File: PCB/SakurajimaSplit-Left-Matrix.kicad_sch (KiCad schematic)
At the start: 42 parts, among them SW10 S, SW11 D, SW12 F, SW13 G, SW14 SW_Push_45deg, SW15 Z, SW16 X, SW17 C, SW18 V, SW19 B, SW2 ESC, SW20 SW_Push_45deg, SW21 SW_Push_45deg, SW22 SW_Push_45deg, SW3 Q, SW4 W, SW5 E, SW6 R, SW7 T, SW8 SW_Push_45deg, SW9 A

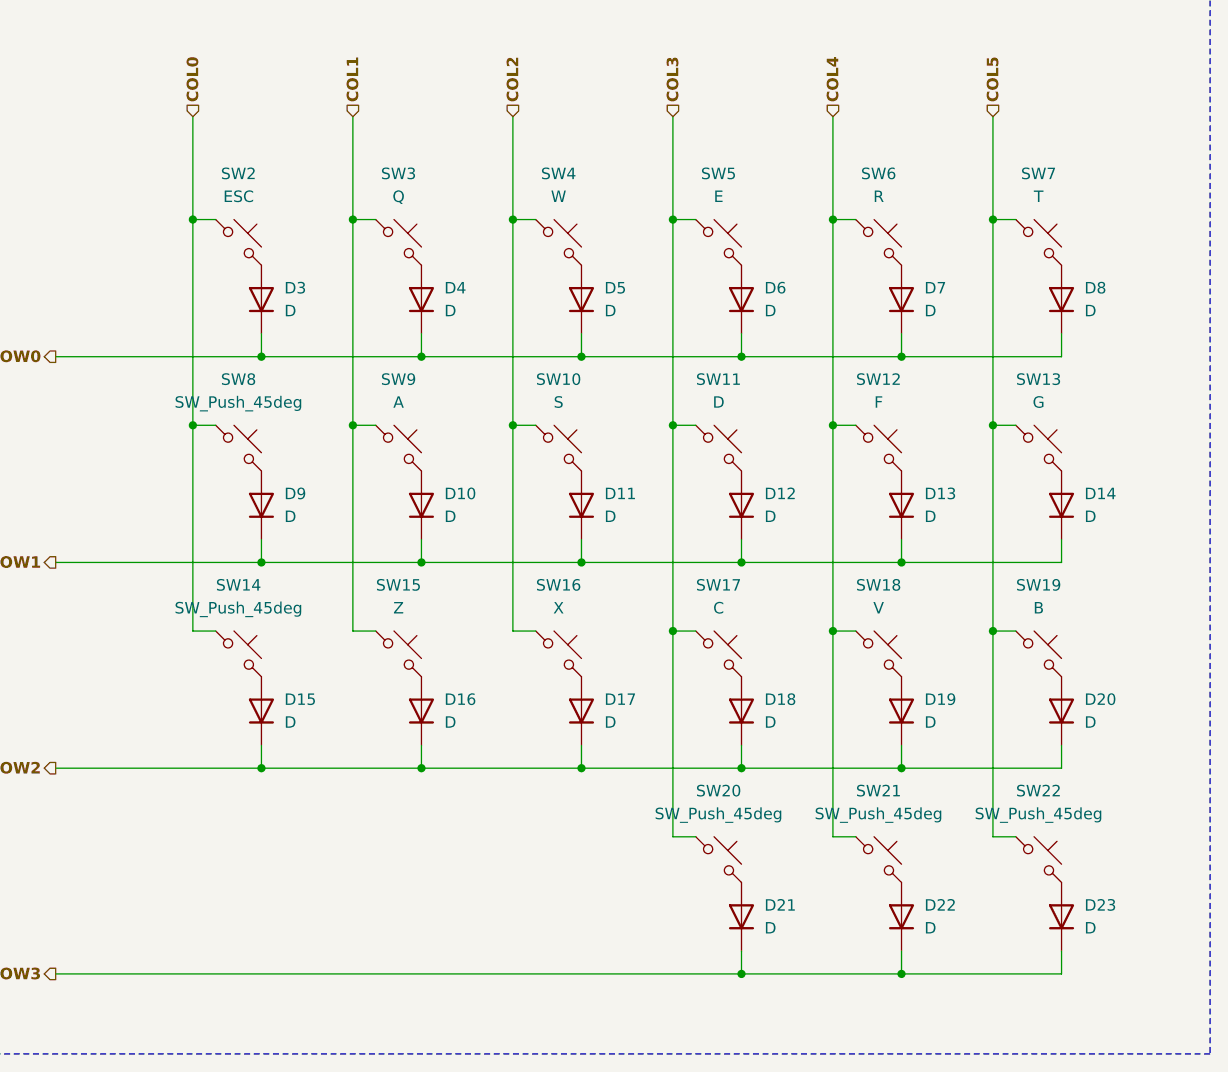
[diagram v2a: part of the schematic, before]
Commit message: feat(sch): cleanup and anotate schematic, choose components
- Fixed mistakes in schematic
- Anotated the schematic
- Found and chose components
- Added GND test points
- Ran ERC and fixed all errors and warnings
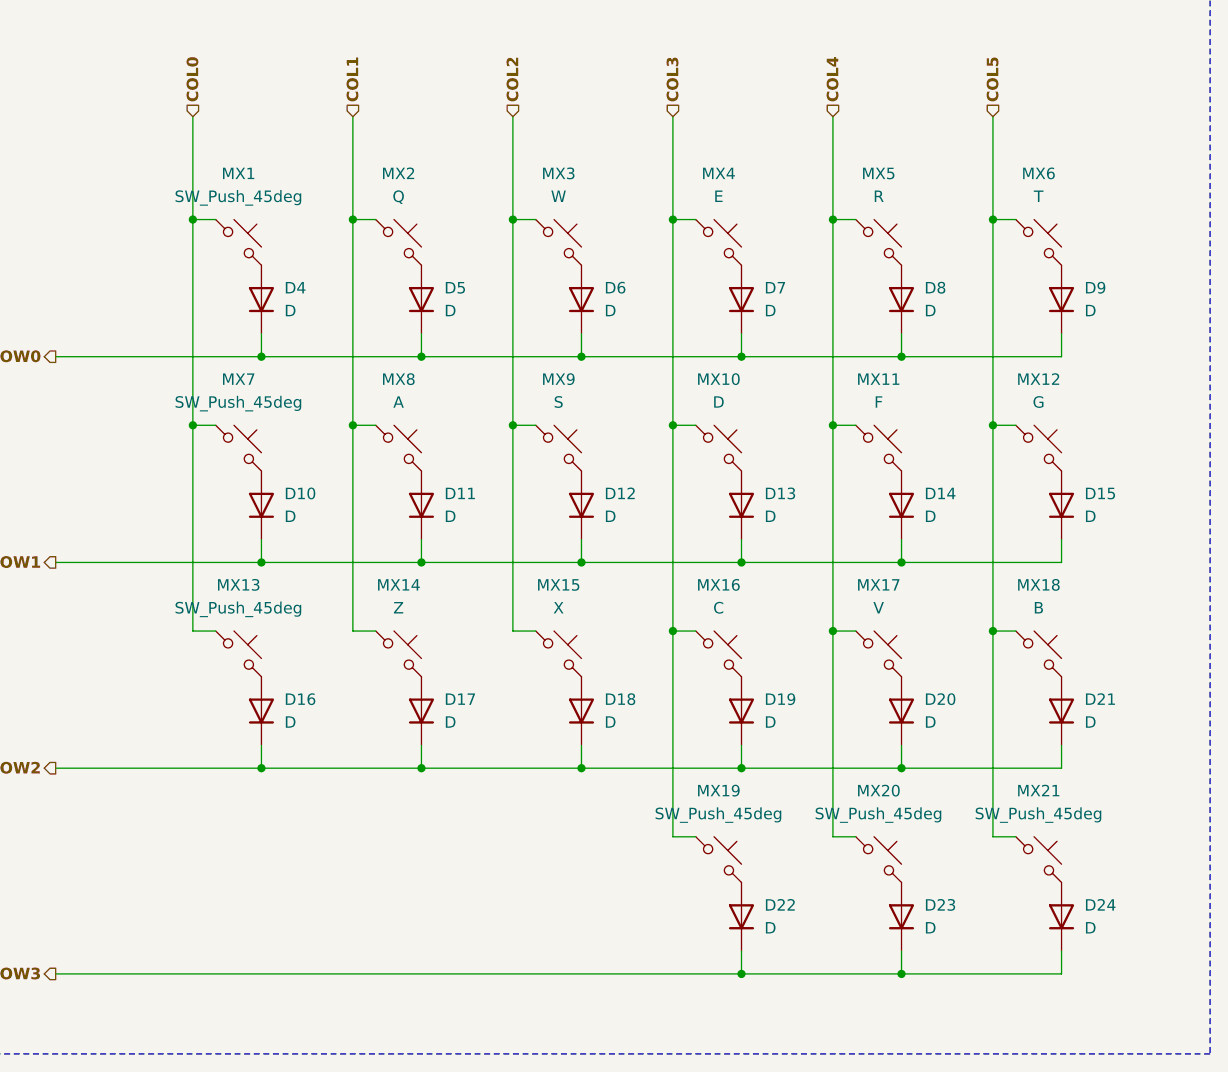
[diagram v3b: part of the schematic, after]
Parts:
- D10: renamed from D9; Distributor Link (none) -> https://lionelectronic.ir/products/2289-1N4148W; Manufacturer (none) -> Jingdao Microelectronics; Manufacturer Part No. (none) -> 1N4148W
- D11: renamed from D10; Distributor Link (none) -> https://lionelectronic.ir/products/2289-1N4148W; Manufacturer (none) -> Jingdao Microelectronics; Manufacturer Part No. (none) -> 1N4148W
- D12: renamed from D11; Distributor Link (none) -> https://lionelectronic.ir/products/2289-1N4148W; Manufacturer (none) -> Jingdao Microelectronics; Manufacturer Part No. (none) -> 1N4148W
- D13: renamed from D12; Distributor Link (none) -> https://lionelectronic.ir/products/2289-1N4148W; Manufacturer (none) -> Jingdao Microelectronics; Manufacturer Part No. (none) -> 1N4148W
- D14: renamed from D13; Distributor Link (none) -> https://lionelectronic.ir/products/2289-1N4148W; Manufacturer (none) -> Jingdao Microelectronics; Manufacturer Part No. (none) -> 1N4148W
- D15: renamed from D14; Distributor Link (none) -> https://lionelectronic.ir/products/2289-1N4148W; Manufacturer (none) -> Jingdao Microelectronics; Manufacturer Part No. (none) -> 1N4148W
- D16: renamed from D15; Distributor Link (none) -> https://lionelectronic.ir/products/2289-1N4148W; Manufacturer (none) -> Jingdao Microelectronics; Manufacturer Part No. (none) -> 1N4148W
- D17: renamed from D16; Distributor Link (none) -> https://lionelectronic.ir/products/2289-1N4148W; Manufacturer (none) -> Jingdao Microelectronics; Manufacturer Part No. (none) -> 1N4148W
- D18: renamed from D17; Distributor Link (none) -> https://lionelectronic.ir/products/2289-1N4148W; Manufacturer (none) -> Jingdao Microelectronics; Manufacturer Part No. (none) -> 1N4148W
- D19: renamed from D18; Distributor Link (none) -> https://lionelectronic.ir/products/2289-1N4148W; Manufacturer (none) -> Jingdao Microelectronics; Manufacturer Part No. (none) -> 1N4148W
- D20: renamed from D19; Distributor Link (none) -> https://lionelectronic.ir/products/2289-1N4148W; Manufacturer (none) -> Jingdao Microelectronics; Manufacturer Part No. (none) -> 1N4148W
- D21: renamed from D20; Distributor Link (none) -> https://lionelectronic.ir/products/2289-1N4148W; Manufacturer (none) -> Jingdao Microelectronics; Manufacturer Part No. (none) -> 1N4148W
- D22: renamed from D21; Distributor Link (none) -> https://lionelectronic.ir/products/2289-1N4148W; Manufacturer (none) -> Jingdao Microelectronics; Manufacturer Part No. (none) -> 1N4148W
- D23: renamed from D22; Distributor Link (none) -> https://lionelectronic.ir/products/2289-1N4148W; Manufacturer (none) -> Jingdao Microelectronics; Manufacturer Part No. (none) -> 1N4148W
- D24: renamed from D23; Distributor Link (none) -> https://lionelectronic.ir/products/2289-1N4148W; Manufacturer (none) -> Jingdao Microelectronics; Manufacturer Part No. (none) -> 1N4148W
- D4: renamed from D3; Distributor Link (none) -> https://lionelectronic.ir/products/2289-1N4148W; Manufacturer (none) -> Jingdao Microelectronics; Manufacturer Part No. (none) -> 1N4148W
- D5: renamed from D4; Distributor Link (none) -> https://lionelectronic.ir/products/2289-1N4148W; Manufacturer (none) -> Jingdao Microelectronics; Manufacturer Part No. (none) -> 1N4148W
- D6: renamed from D5; Distributor Link (none) -> https://lionelectronic.ir/products/2289-1N4148W; Manufacturer (none) -> Jingdao Microelectronics; Manufacturer Part No. (none) -> 1N4148W
- D7: renamed from D6; Distributor Link (none) -> https://lionelectronic.ir/products/2289-1N4148W; Manufacturer (none) -> Jingdao Microelectronics; Manufacturer Part No. (none) -> 1N4148W
- D8: renamed from D7; Distributor Link (none) -> https://lionelectronic.ir/products/2289-1N4148W; Manufacturer (none) -> Jingdao Microelectronics; Manufacturer Part No. (none) -> 1N4148W
- D9: renamed from D8; Distributor Link (none) -> https://lionelectronic.ir/products/2289-1N4148W; Manufacturer (none) -> Jingdao Microelectronics; Manufacturer Part No. (none) -> 1N4148W
- MX1: renamed from SW2; value ESC -> SW_Push_45deg; now left out of the parts list
- MX10: renamed from SW11; now left out of the parts list
- MX11: renamed from SW12; now left out of the parts list
- MX12: renamed from SW13; now left out of the parts list
- MX13: renamed from SW14; now left out of the parts list
- MX14: renamed from SW15; now left out of the parts list
- MX15: renamed from SW16; now left out of the parts list
- MX16: renamed from SW17; now left out of the parts list
- MX17: renamed from SW18; now left out of the parts list
- MX18: renamed from SW19; now left out of the parts list
- MX19: renamed from SW20; now left out of the parts list
- MX2: renamed from SW3; now left out of the parts list
- MX20: renamed from SW21; now left out of the parts list
- MX21: renamed from SW22; now left out of the parts list
- MX3: renamed from SW4; now left out of the parts list
- MX4: renamed from SW5; now left out of the parts list
- MX5: renamed from SW6; now left out of the parts list
- MX6: renamed from SW7; now left out of the parts list
- MX7: renamed from SW8; now left out of the parts list
- MX8: renamed from SW9; now left out of the parts list
- MX9: renamed from SW10; now left out of the parts list
